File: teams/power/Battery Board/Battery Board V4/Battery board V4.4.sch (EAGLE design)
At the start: 49 parts, among them Q1 TRANS_NPN-MMBT2222AL

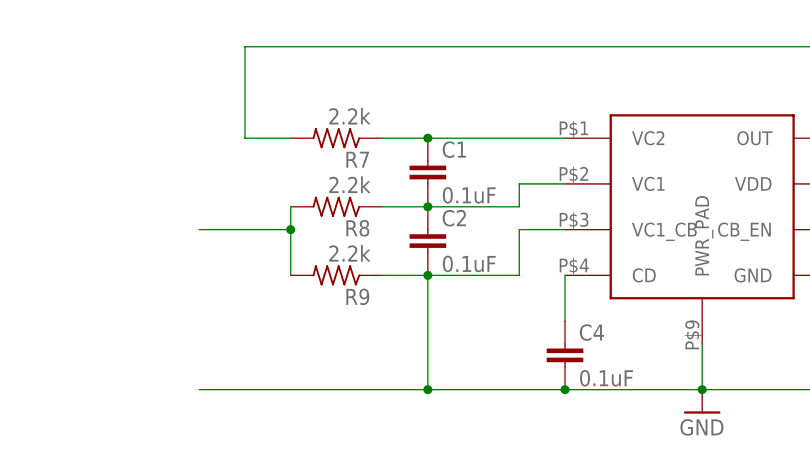
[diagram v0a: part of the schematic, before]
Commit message: Minor changes to battery board V4.3 and tracking V4.4 with battery ballancer fix in progress/
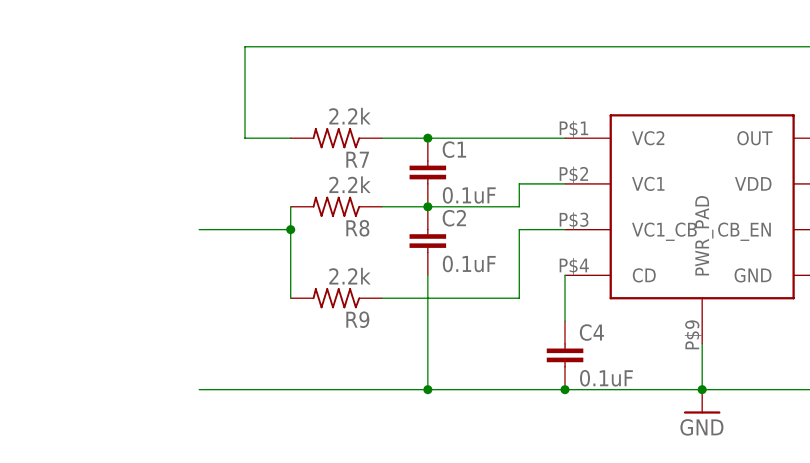
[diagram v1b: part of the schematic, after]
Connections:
- new net N$36: R9.1, U$8.VC1_CB
- net GND: no longer R9.1, U$8.VC1_CB
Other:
- moved on the sheet: R9
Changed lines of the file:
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@@
 <instance part="C1" gate="G$1" x="134.62" y="22.86"/>
 <instance part="C2" gate="G$1" x="134.62" y="15.24"/>
-<instance part="R9" gate="G$1" x="124.46" y="10.16" rot="R180"/>
+<instance part="R9" gate="G$1" x="124.46" y="7.62" rot="R180"/>
 <instance part="C3" gate="G$1" x="213.36" y="12.7"/>
 <instance part="C4" gate="G$1" x="149.86" y="2.54"/>
@@
 <pinref part="R9" gate="G$1" pin="2"/>
 <wire x1="119.38" y1="17.78" x2="119.38" y2="15.24" width="0.1524" layer="91"/>
-<wire x1="119.38" y1="15.24" x2="119.38" y2="10.16" width="0.1524" layer="91"/>
+<wire x1="119.38" y1="15.24" x2="119.38" y2="7.62" width="0.1524" layer="91"/>
 <junction x="119.38" y="15.24"/>
 <wire x1="119.38" y1="15.24" x2="109.22" y2="15.24" width="0.1524" layer="91"/>
@@
 </segment>
 <segment>
-<wire x1="149.86" y1="15.24" x2="144.78" y2="15.24" width="0.1524" layer="91"/>
-<wire x1="144.78" y1="15.24" x2="144.78" y2="10.16" width="0.1524" layer="91"/>
 <pinref part="C2" gate="G$1" pin="2"/>
-<wire x1="144.78" y1="10.16" x2="134.62" y2="10.16" width="0.1524" layer="91"/>
-<pinref part="R9" gate="G$1" pin="1"/>
-<wire x1="134.62" y1="10.16" x2="129.54" y2="10.16" width="0.1524" layer="91"/>
-<junction x="134.62" y="10.16"/>
 <wire x1="134.62" y1="10.16" x2="134.62" y2="-2.54" width="0.1524" layer="91"/>
 <pinref part="C4" gate="G$1" pin="2"/>
@@
 <wire x1="134.62" y1="-2.54" x2="109.22" y2="-2.54" width="0.1524" layer="91"/>
 <junction x="134.62" y="-2.54"/>
-<pinref part="U$8" gate="G$1" pin="VC1_CB"/>
 <pinref part="U$8" gate="G$1" pin="GND"/>
 <pinref part="U$8" gate="G$1" pin="PWR_PAD"/>
@@
 </segment>
 </net>
+<net name="N$36" class="0">
+<segment>
+<pinref part="U$8" gate="G$1" pin="VC1_CB"/>
+<wire x1="149.86" y1="15.24" x2="144.78" y2="15.24" width="0.1524" layer="91"/>
+<wire x1="144.78" y1="15.24" x2="144.78" y2="7.62" width="0.1524" layer="91"/>
+<pinref part="R9" gate="G$1" pin="1"/>
+<wire x1="129.54" y1="7.62" x2="144.78" y2="7.62" width="0.1524" layer="91"/>
+</segment>
+</net>

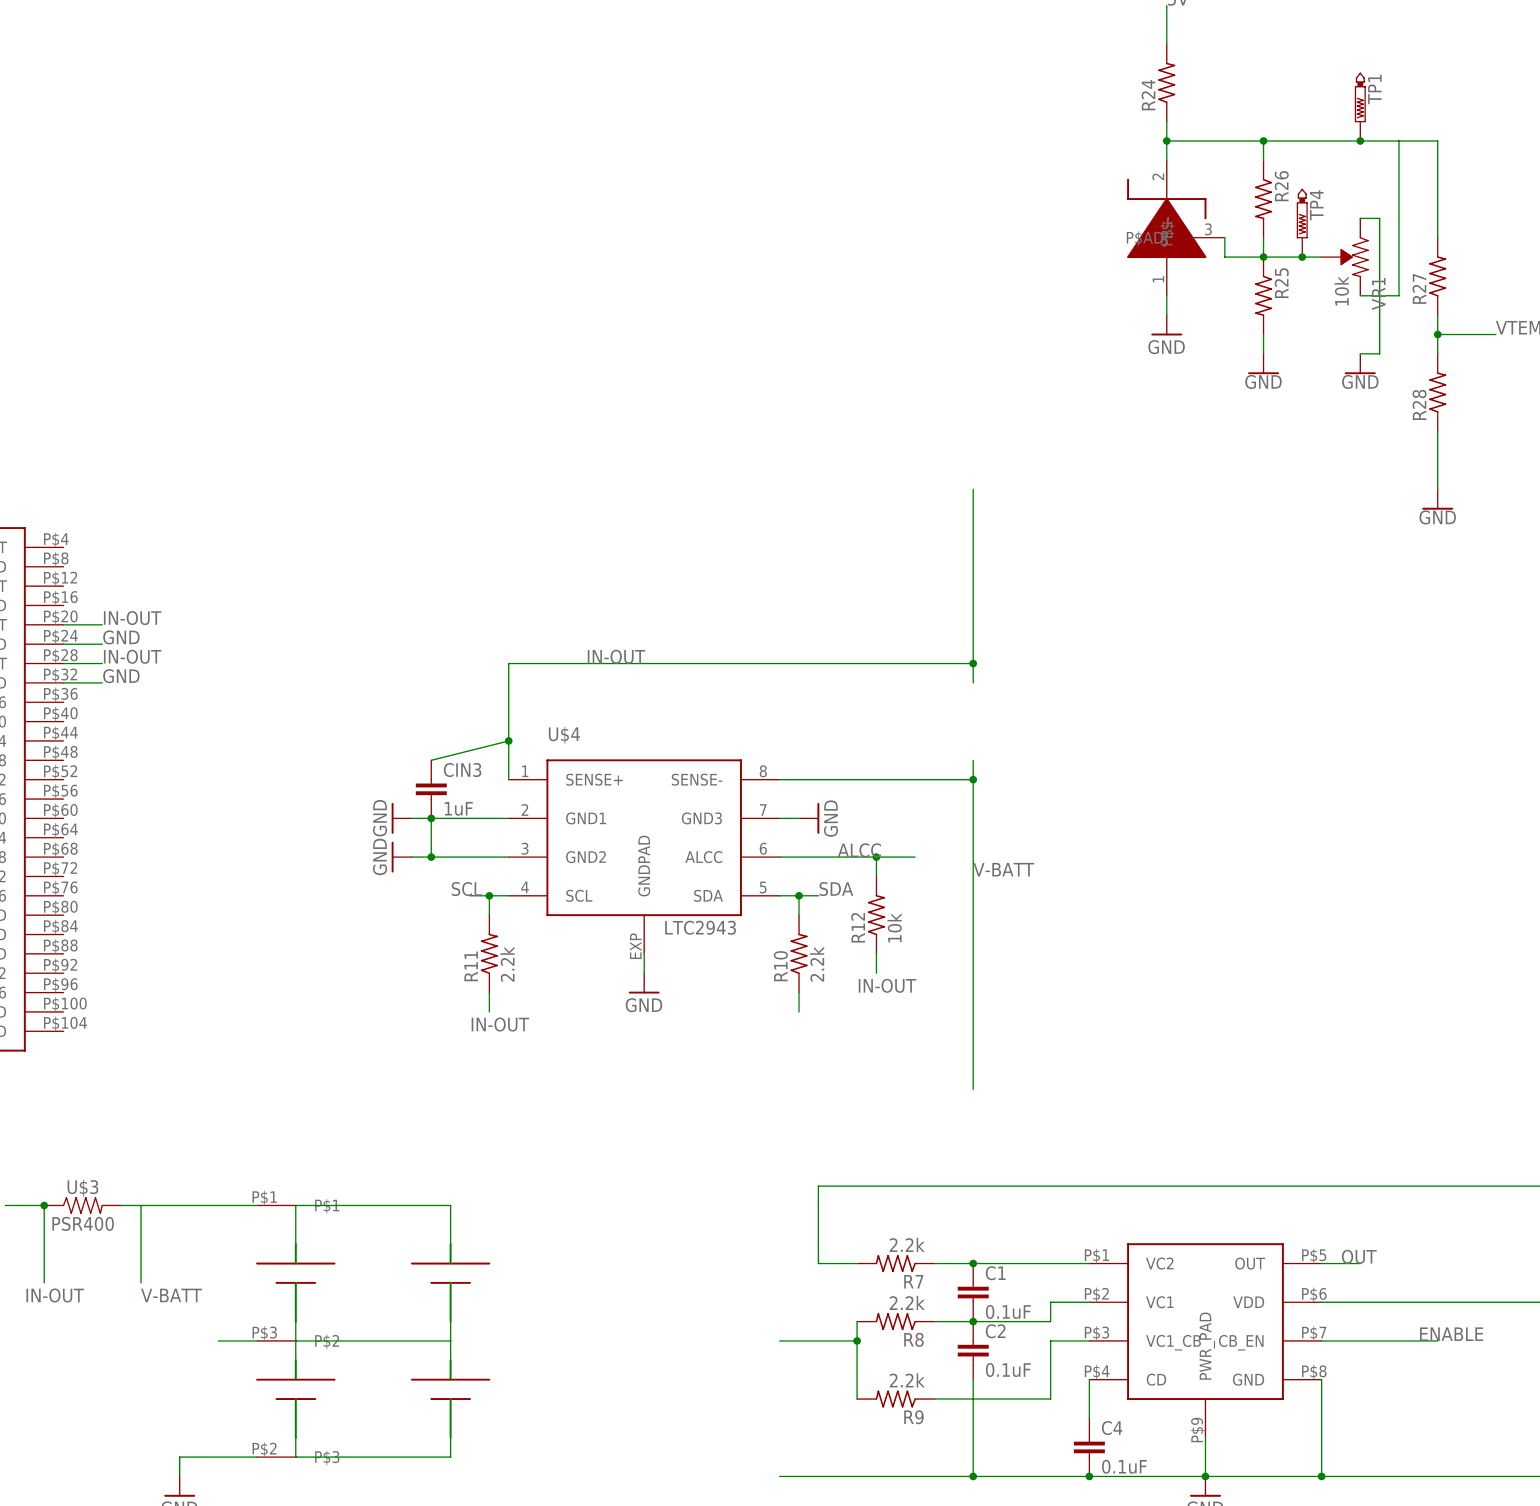
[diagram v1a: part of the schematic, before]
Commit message: EPS / Battery board: Set design rules and fixed clearance errors.
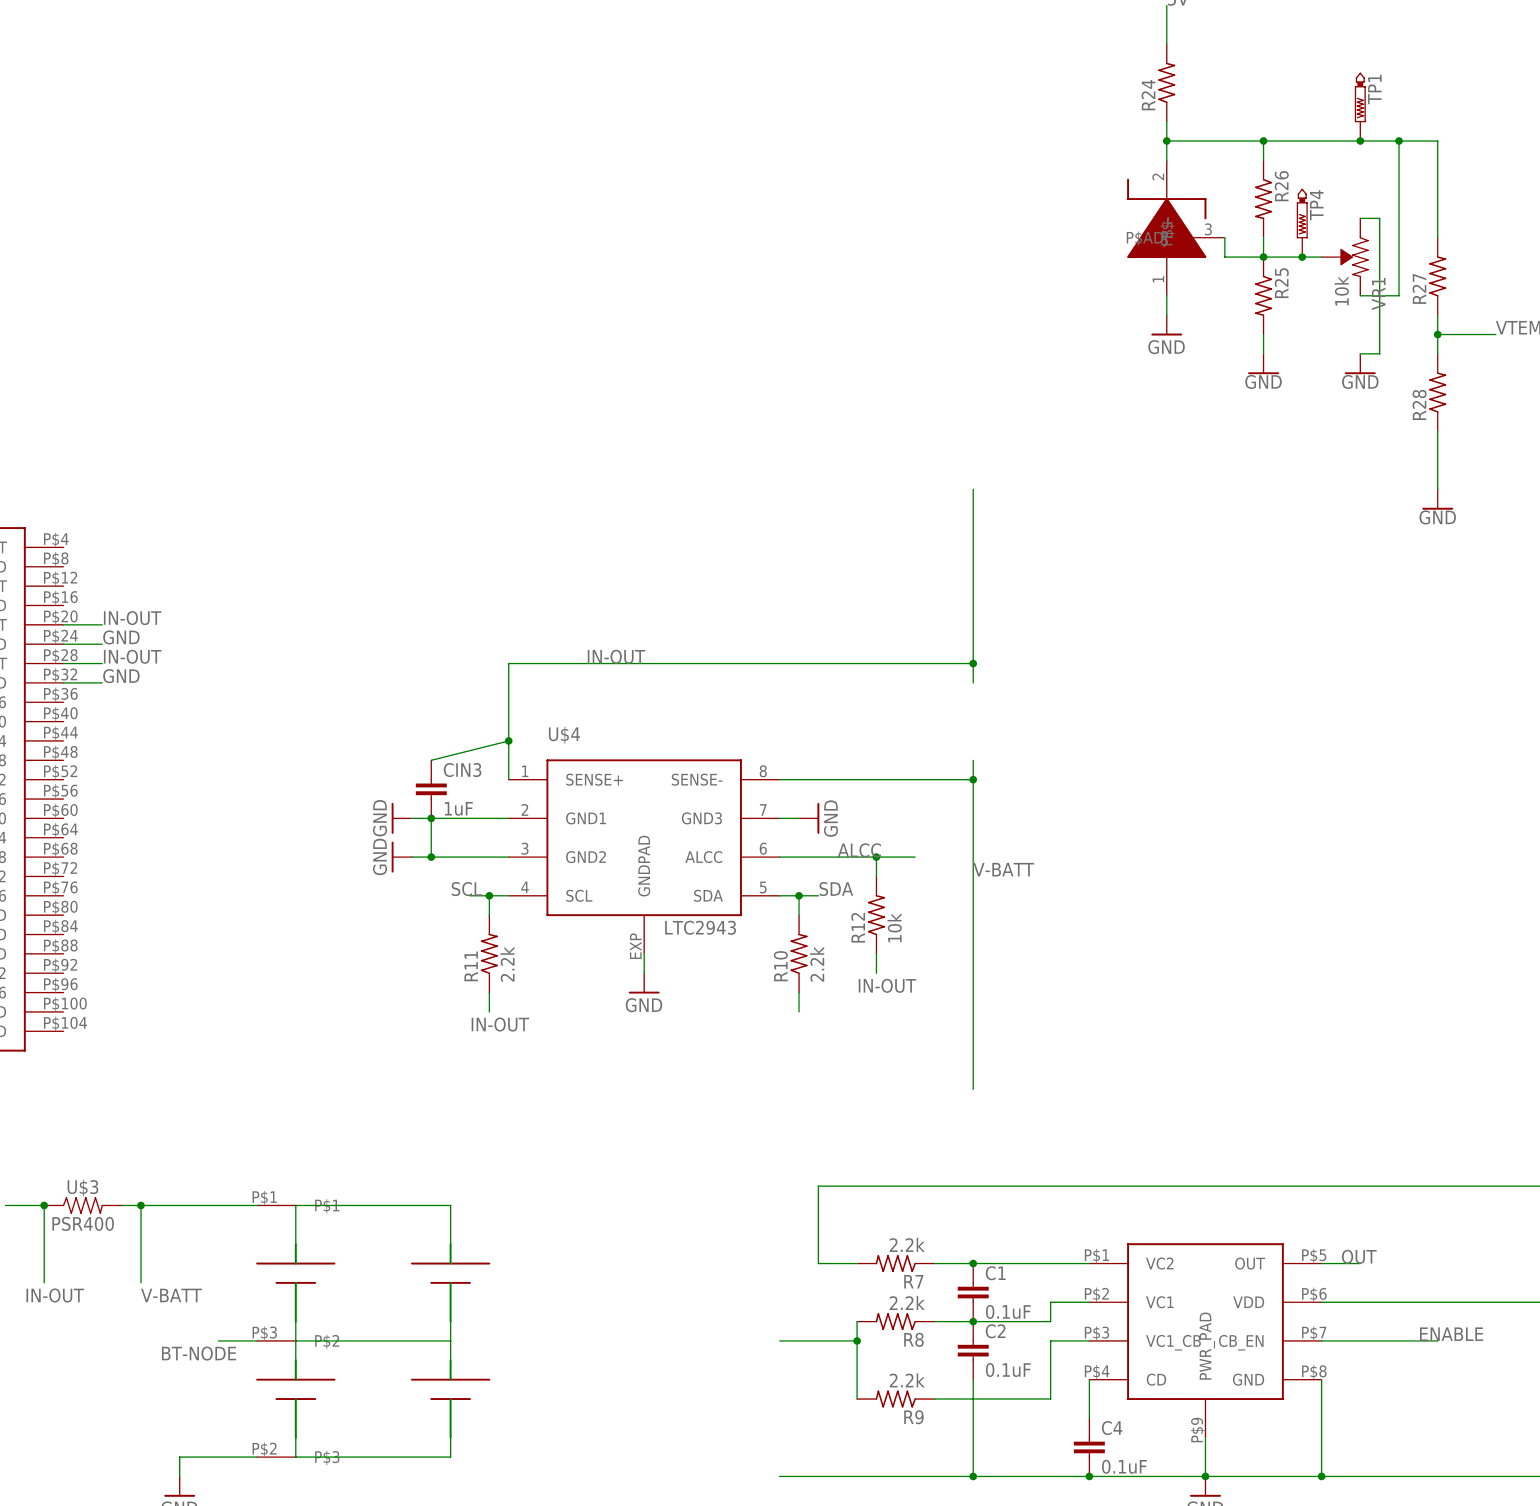
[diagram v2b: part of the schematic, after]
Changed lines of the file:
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@@
 <pinref part="U$6" gate="G$1" pin="P$2"/>
 <wire x1="40.64" y1="15.24" x2="35.56" y2="15.24" width="0.1524" layer="91"/>
+<label x="27.94" y="12.7" size="1.778" layer="95"/>
 </segment>
 </net>
@@
 <pinref part="U$6" gate="G$1" pin="P$1"/>
 <wire x1="25.4" y1="33.02" x2="40.64" y2="33.02" width="0.1524" layer="91"/>
+<junction x="25.4" y="33.02"/>
 </segment>
 <segment>
@@
 <pinref part="TP1" gate="G$1" pin="TP"/>
 <junction x="185.42" y="172.72"/>
+<junction x="190.5" y="172.72"/>
 </segment>
 </net>
@@
 </sheet>
 </sheets>
+<errors>
+</errors>
 </schematic>
 </drawing>
